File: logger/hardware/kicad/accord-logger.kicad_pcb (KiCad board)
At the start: 2 copper layers, 120 x 80 mm, 60 parts, among them J1 Board connector 14-way, J3 Spare GP13 / switched power, J4 Reset RUN-GND, J5 SD breakout 6-way, Q5 IPD50P04P4L-11, Q6 2N3904, Q7 2N3904, U1 RaspberryPi_Pico_W, U15 MAX3485, U16 DS3231SN, U6 LM2678T-5.0

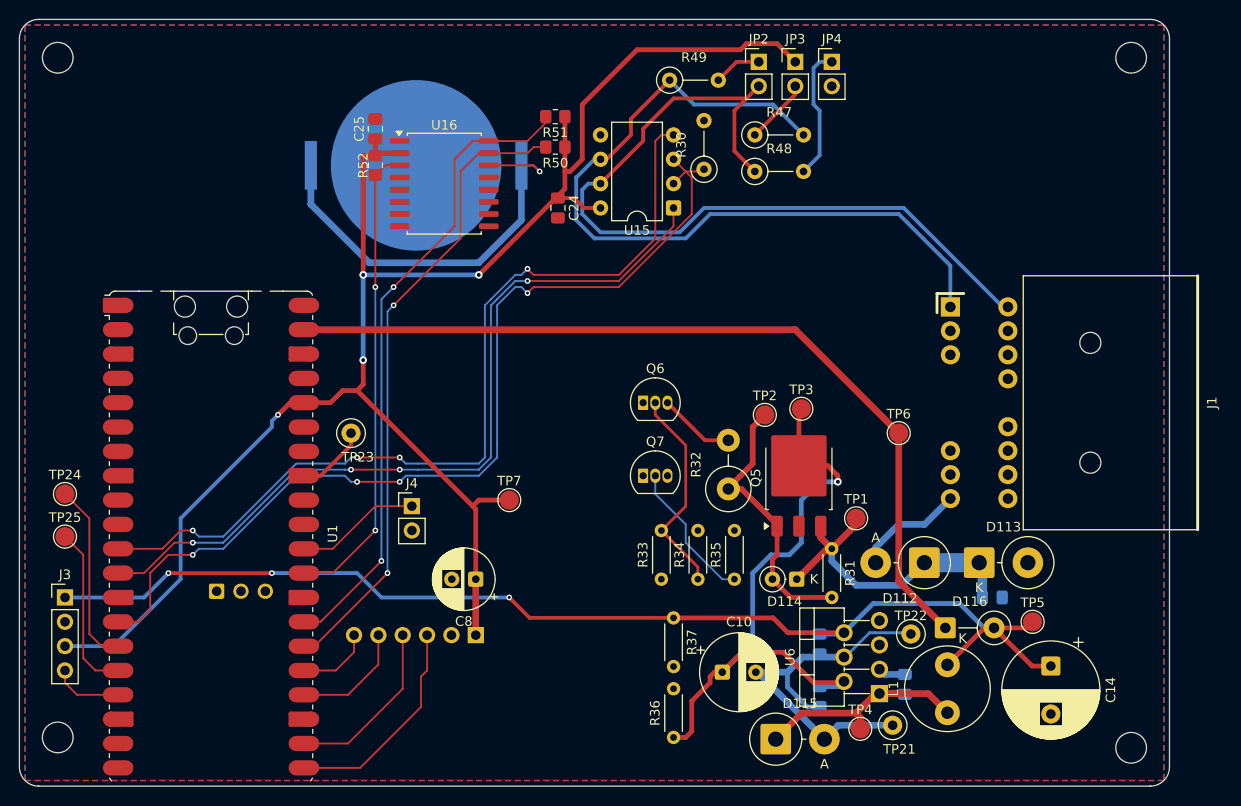
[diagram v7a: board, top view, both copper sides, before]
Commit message: layout: in_tach, in_brake and in_fuel placed and routed
Owner switched on the three input steps (nine on_board flags) and placed
them with the D-THT-15 through-hole parts. After review: ground vias tie
the U16 pin 13 and C24 pin 2 front islands to the back pour; FUEL_ADC
cleared of the UART/DE vias; AGND routed as its own trace (Pico pin 33,
J1.10, R8, D105, C1, TP23; 139 mm); 3V3 to the D102/D103 cathodes; the
tach and brake clamps moved to the Pico's left strip by GP3/GP4; R9, D104
and D105 moved toward C1 (FUEL_ADC run now about 27 mm, was 80).
SUPPLY_ADC via and VSS_IN stub are intentional pre-routing.

Refilled scratch DRC: parity 0, no clearance errors, nothing unconnected
but Q5's middle lead. Open: starved thermal relief on J1 pin 2 (bus GND)
and Q6 pin 1 (QI emitter).

Claude-Session-ID: 42dd0e33-28b5-4936-847e-9c2e1d2488fa
Co-Authored-By: Claude Opus 5.5 <noreply@anthropic.com>
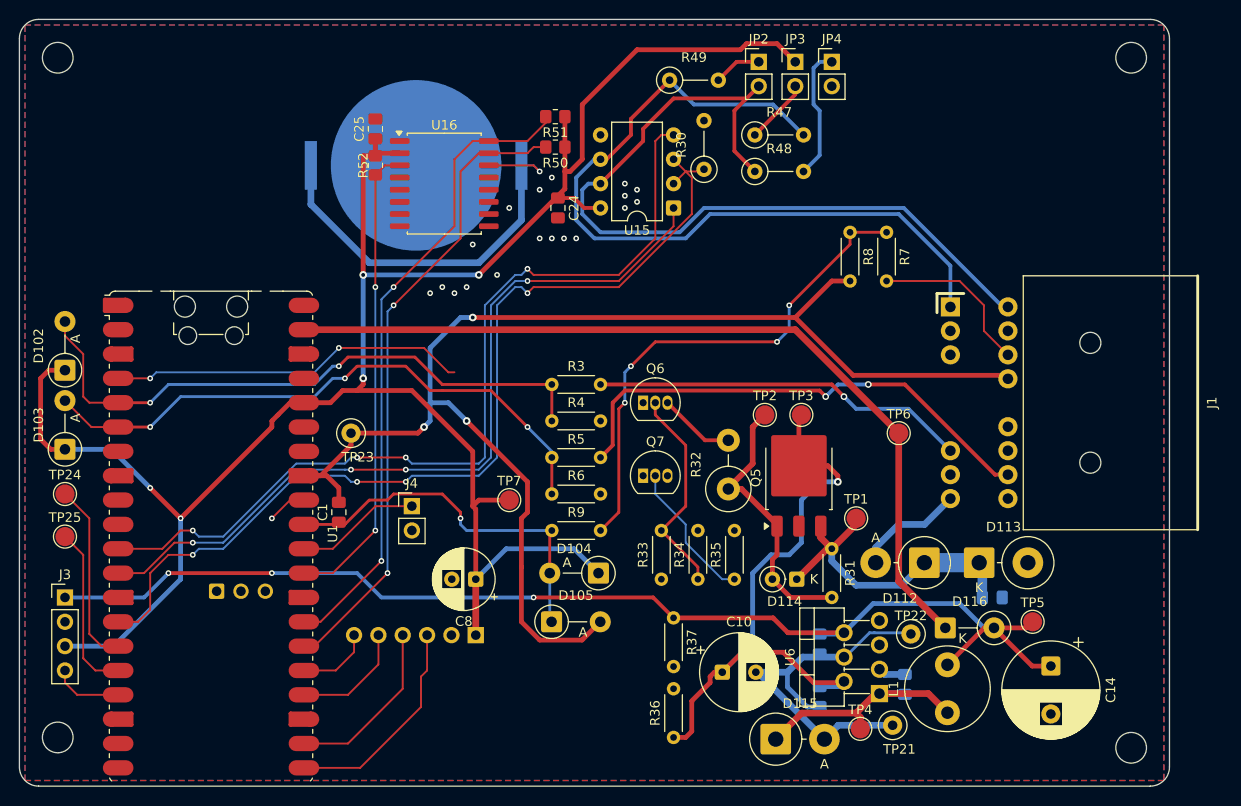
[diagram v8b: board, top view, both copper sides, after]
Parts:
- added C1: 1uF, Capacitor_SMD:C_0805_2012Metric_Pad1.18x1.45mm_HandSolder, F.Cu at (121.9, 111.1)
- added D102: 1N5819, Diode_THT:D_DO-41_SOD81_P5.08mm_Vertical_AnodeUp, F.Cu at (93.3, 96.3)
- added D103: 1N5819, Diode_THT:D_DO-41_SOD81_P5.08mm_Vertical_AnodeUp, F.Cu at (93.3, 104.6)
- added D104: 1N5819, Diode_THT:D_DO-41_SOD81_P5.08mm_Vertical_AnodeUp, F.Cu at (149.0, 117.5)
- added D105: 1N5819, Diode_THT:D_DO-41_SOD81_P5.08mm_Vertical_AnodeUp, F.Cu at (144.1, 122.6)
- added R3: 22k, Resistor_THT:R_Axial_DIN0204_L3.6mm_D1.6mm_P5.08mm_Horizontal, F.Cu at (149.2, 97.8)
- added R4: 6.8k, Resistor_THT:R_Axial_DIN0204_L3.6mm_D1.6mm_P5.08mm_Horizontal, F.Cu at (144.1, 101.6)
- added R5: 22k, Resistor_THT:R_Axial_DIN0204_L3.6mm_D1.6mm_P5.08mm_Horizontal, F.Cu at (149.2, 105.4)
- added R6: 6.8k, Resistor_THT:R_Axial_DIN0204_L3.6mm_D1.6mm_P5.08mm_Horizontal, F.Cu at (144.1, 109.2)
- added R7: 7.5k, Resistor_THT:R_Axial_DIN0204_L3.6mm_D1.6mm_P5.08mm_Horizontal, F.Cu at (179.1, 87.0)
- added R8: 4.7k, Resistor_THT:R_Axial_DIN0204_L3.6mm_D1.6mm_P5.08mm_Horizontal, F.Cu at (175.3, 81.9)
- added R9: 1k, Resistor_THT:R_Axial_DIN0204_L3.6mm_D1.6mm_P5.08mm_Horizontal, F.Cu at (149.2, 113.0)
- moved TP3 0.64 mm to (170.2, 101.0)
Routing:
- net /AGND: track 7.50 -> 139.4 mm, vias 0 -> 3
- net /TACH_IN: track 0.00 -> 64.8 mm, vias 0 -> 2
- net /BRAKE_IN: track 0.00 -> 62.7 mm, vias 0 -> 3
- net /FUEL_DIV: track 0.00 -> 53.1 mm, vias 0 -> 4
- net /C14_TAP: track 0.00 -> 52.7 mm, vias 0 -> 2
- net /P3V3_SW: track 181.7 -> 227.8 mm, vias 4 -> 5
- net /B1_TAP: track 0.00 -> 39.4 mm, vias 0 -> 1
- net /FUEL_ADC: track 0.00 -> 39.2 mm, vias 0 -> 1
- net /VSS_IN: track 0.00 -> 37.5 mm, vias 0 -> 2
- net /C11_TAP: track 0.00 -> 17.5 mm
- net /SUPPLY_ADC: track 0.00 -> 4.13 mm, vias 0 -> 1
- net /PGND: vias 0 -> 18
